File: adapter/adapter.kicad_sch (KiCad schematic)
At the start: 13 parts, among them J1 DF3A-2P-2DSA, J10 Ribbon, J11 Ribbon, J12 Ribbon, J9 Ribbon, SW1 CAS-120TA, U1 nice_nano, U2 nice_nano

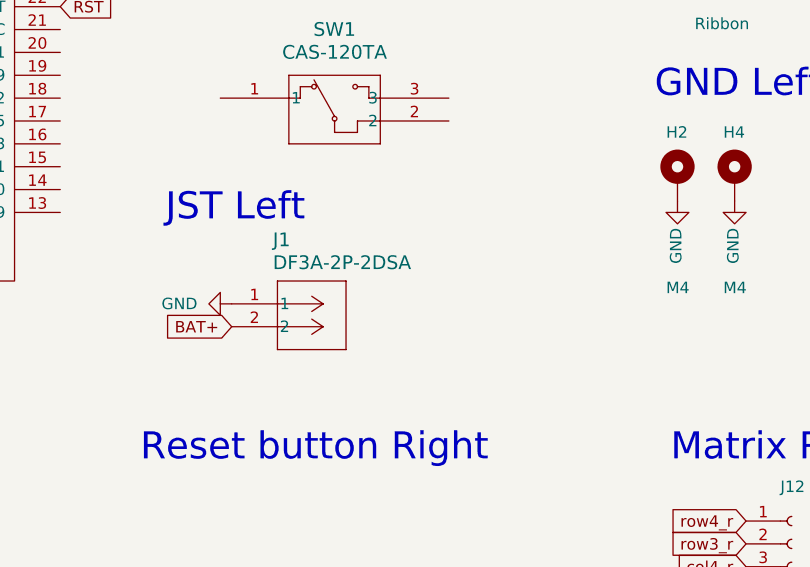
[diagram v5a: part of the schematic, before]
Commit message: Place all the components onto the pcb
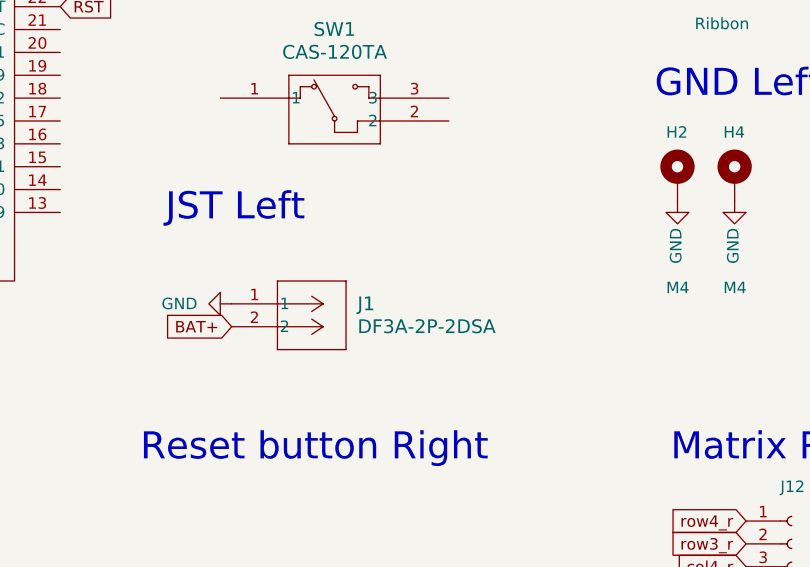
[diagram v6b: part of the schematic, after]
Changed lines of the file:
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@@
+	)
+	(symbol
+		(lib_id "DF3A_2P_2DSA:DF3A-2P-2DSA")
+		(at 85.09 82.55 0)
+		(unit 1)
+		(exclude_from_sim no)
+		(in_bom yes)
+		(on_board yes)
+		(dnp no)
+		(fields_autoplaced yes)
+		(property "Reference" "J1"
+			(at 99.06 82.5499 0)
+			(effects
+				(font
+					(size 1.524 1.524)
+				)
+				(justify left)
+			)
+		)
+		(property "Value" "DF3A-2P-2DSA"
+			(at 99.06 85.0899 0)
+			(effects
+				(font
+					(size 1.524 1.524)
+				)
+				(justify left)
+			)
+		)
+		(property "Footprint" "Library:DF3A_2P_2DSA"
+			(at 85.09 82.55 0)
+			(effects
+				(font
+					(size 1.27 1.27)
+					(italic yes)
+				)
+				(hide yes)
+			)
+		)
+		(property "Datasheet" "DF3A-2P-2DSA"
+			(at 85.09 82.55 0)
+			(effects
+				(font
+					(size 1.27 1.27)
+					(italic yes)
+				)
+				(hide yes)
+			)
+		)
+		(property "Description" ""
+			(at 85.09 82.55 0)
+			(effects
+				(font
+					(size 1.27 1.27)
+				)
+				(hide yes)
+			)
+		)
+		(pin "2"
+		)
+		(pin "1"
+		)
+		(instances
+			(project ""
+				(path "/e63e39d7-6ac0-4ffd-8aa3-1841a4541b55"
+					(reference "J1")
+					(unit 1)
+				)
+			)
+		)
 	)
 	(symbol
@@
 					(unit 1)
 				)
-			)
-		)
-	)
-	(symbol
-		(lib_id "DF3A_2P_2DSA:DF3A-2P-2DSA")
-		(at 85.09 82.55 0)
-		(unit 1)
-		(exclude_from_sim no)
-		(in_bom yes)
-		(on_board yes)
-		(dnp no)
-		(property "Reference" "J1"
-			(at 89.662 75.438 0)
-			(effects
-				(font
-					(size 1.524 1.524)
-				)
-				(justify left)
-			)
-		)
-		(property "Value" "DF3A-2P-2DSA"
-			(at 89.662 77.978 0)
-			(effects
-				(font
-					(size 1.524 1.524)
-				)
-				(justify left)
-			)
-		)
-		(property "Footprint" "Library:DF3A_2P_2DSA"
-			(at 85.09 82.55 0)
-			(effects
-				(font
-					(size 1.27 1.27)
-					(italic yes)
-				)
-				(hide yes)
-			)
-		)
-		(property "Datasheet" "DF3A-2P-2DSA"
-			(at 85.09 82.55 0)
-			(effects
-				(font
-					(size 1.27 1.27)
-					(italic yes)
-				)
-				(hide yes)
-			)
-		)
-		(property "Description" ""
-			(at 85.09 82.55 0)
-			(effects
-				(font
-					(size 1.27 1.27)
-				)
-				(hide yes)
-			)
-		)
-		(pin "1"
-		)
-		(pin "2"
-		)
-		(instances
-			(project ""
-				(path "/e63e39d7-6ac0-4ffd-8aa3-1841a4541b55"
-					(reference "J1")
-					(unit 1)
-				)
